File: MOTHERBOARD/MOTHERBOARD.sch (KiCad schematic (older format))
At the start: 92 parts, among them J101 Conn_02x05_Odd_Even, J102 Conn_02x05_Odd_Even, J103 Conn_02x05_Odd_Even, J104 Conn_02x05_Odd_Even, J105 Conn_02x05_Odd_Even, J106 Conn_02x05_Odd_Even, J107 Conn_02x05_Odd_Even, J108 Conn_02x05_Odd_Even, J109 Conn_02x05_Odd_Even, J110 Conn_02x05_Odd_Even, J111 Conn_02x05_Odd_Even, J112 Conn_02x05_Odd_Even, J113 Conn_02x05_Odd_Even, J114 Conn_02x05_Odd_Even, J115 Conn_02x05_Odd_Even, J116 Conn_02x05_Odd_Even, J117 Conn_02x05_Odd_Even, J118 Conn_02x05_Odd_Even, J119 Conn_02x02_Odd_Even, U101 TL072

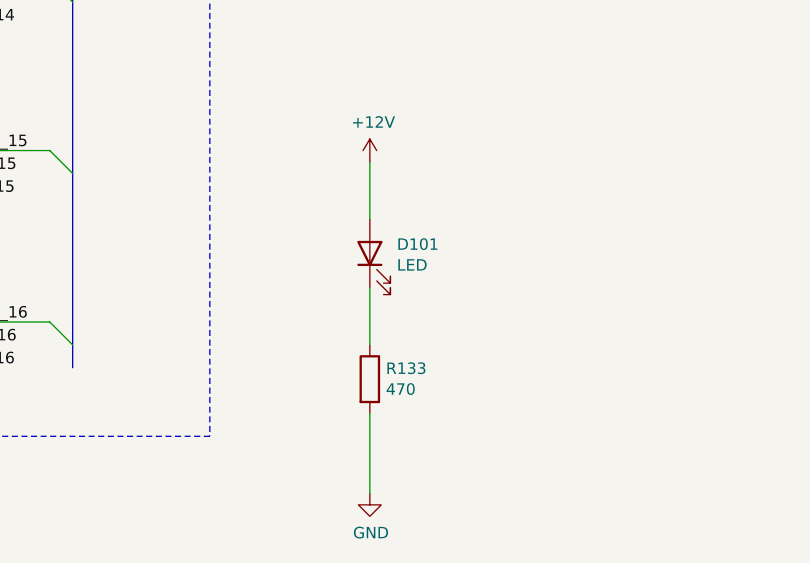
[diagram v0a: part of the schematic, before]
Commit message: New series resistor values for LEDs
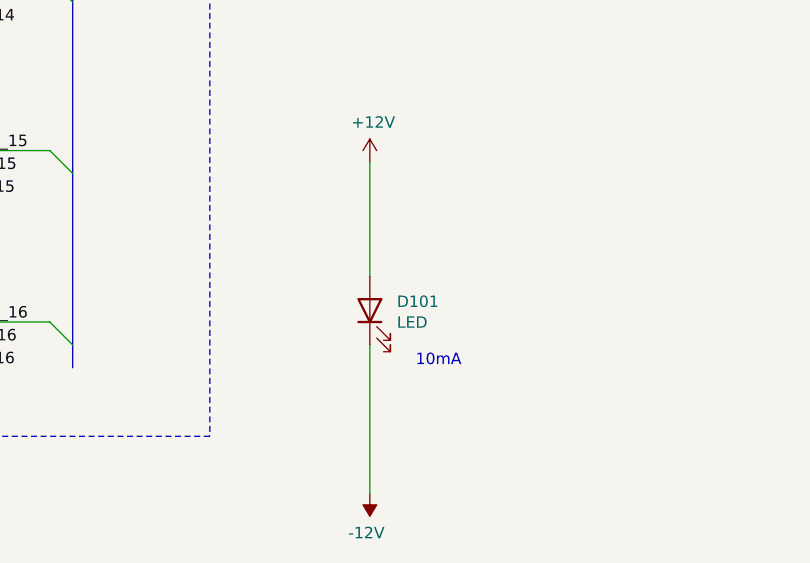
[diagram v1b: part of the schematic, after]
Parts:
- removed R133: 470, Resistor_SMD:R_0603_1608Metric_Pad0.98x0.95mm_HandSolder, symbol Device:R
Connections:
- net -12V: now also D101.1 (K)
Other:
- note added: "10mA"
- moved on the sheet: D101
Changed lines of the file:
@@
 $EndComp
 Wire Wire Line
-	7050 12200 7050 12450
-$Comp
-L Device:R R?
-U 1 1 61805BAC
-P 7050 13150
-AR Path="/626F2161/61805BAC" Ref="R?"  Part="1"
-AR Path="/61805BAC" Ref="R133"  Part="1"
-F 0 "R133" H 7120 13196 50  0000 L CNN
-F 1 "470" H 7120 13105 50  0000 L CNN
-F 2 "Resistor_SMD:R_0603_1608Metric_Pad0.98x0.95mm_HandSolder" V 6980 13150 50  0001 C CNN
-F 3 "~" H 7050 13150 50  0001 C CNN
-	1    7050 13150
-	1    0    0    -1
-$EndComp
-Wire Wire Line
-	7050 12750 7050 13000
-Wire Wire Line
-	7050 13300 7050 13650
-$Comp
-L power:GND #PWR?
-U 1 1 61805BB4
-P 7050 13650
-AR Path="/626F2161/61805BB4" Ref="#PWR?"  Part="1"
-AR Path="/61805BB4" Ref="#PWR0195"  Part="1"
-F 0 "#PWR0195" H 7050 13400 50  0001 C CNN
-F 1 "GND" H 7055 13477 50  0000 C CNN
-F 2 "" H 7050 13650 50  0001 C CNN
-F 3 "" H 7050 13650 50  0001 C CNN
-	1    7050 13650
-	1    0    0    -1
-$EndComp
+	7050 12200 7050 12700
 $Comp
 L Device:LED D?
 U 1 1 61805BBA
-P 7050 12600
+P 7050 12850
 AR Path="/626F2161/61805BBA" Ref="D?"  Part="1"
 AR Path="/61805BBA" Ref="D101"  Part="1"
-F 0 "D101" V 7089 12482 50  0000 R CNN
-F 1 "LED" V 6998 12482 50  0000 R CNN
-F 2 "OHMCODER:TE-6-440054-3" H 7050 12600 50  0001 C CNN
-F 3 "~" H 7050 12600 50  0001 C CNN
-	1    7050 12600
+F 0 "D101" V 7089 12732 50  0000 R CNN
+F 1 "LED" V 6998 12732 50  0000 R CNN
+F 2 "OHMCODER:TE-6-440054-3" H 7050 12850 50  0001 C CNN
+F 3 "~" H 7050 12850 50  0001 C CNN
+	1    7050 12850
 	0    -1   -1   0
 $EndComp
@@
 	-1   0    0    1
 $EndComp
+Wire Wire Line
+	7050 13000 7050 13650
 Wire Bus Line
 	5750 1300 5750 13100
@@
 Wire Bus Line
 	13200 1050 13200 7200
+$Comp
+L power:-12V #PWR?
+U 1 1 61C219D3
+P 7050 13650
+F 0 "#PWR?" H 7050 13750 50  0001 C CNN
+F 1 "-12V" H 7065 13823 50  0000 C CNN
+F 2 "" H 7050 13650 50  0001 C CNN
+F 3 "" H 7050 13650 50  0001 C CNN
+	1    7050 13650
+	-1   0    0    1
+$EndComp
+Text Notes 7250 13100 0    50   ~ 0
+10mA
 $EndSCHEMATC
